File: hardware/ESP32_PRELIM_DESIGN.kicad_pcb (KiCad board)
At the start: 2 copper layers, 70 parts, among them J1 Conn_01x11_Socket, J4 Conn_01x02_Pin, J5 USB_C_Receptacle_USB2.0_16P, J6 Conn_01x05_Pin, J7 Conn_01x05_Pin, Q1 2N7002, SW1 SW_Push, SW2 SW_Push, SW3 SW_Push, U1 ESP32-S3-WROOM-1, U10 BQ24075RGT, U11 MAX98357A, U12 USBLC6-2SC6, U2 DRV2605LDGS, U3 TPS63020DSJR, U4 MAX17048G_T10

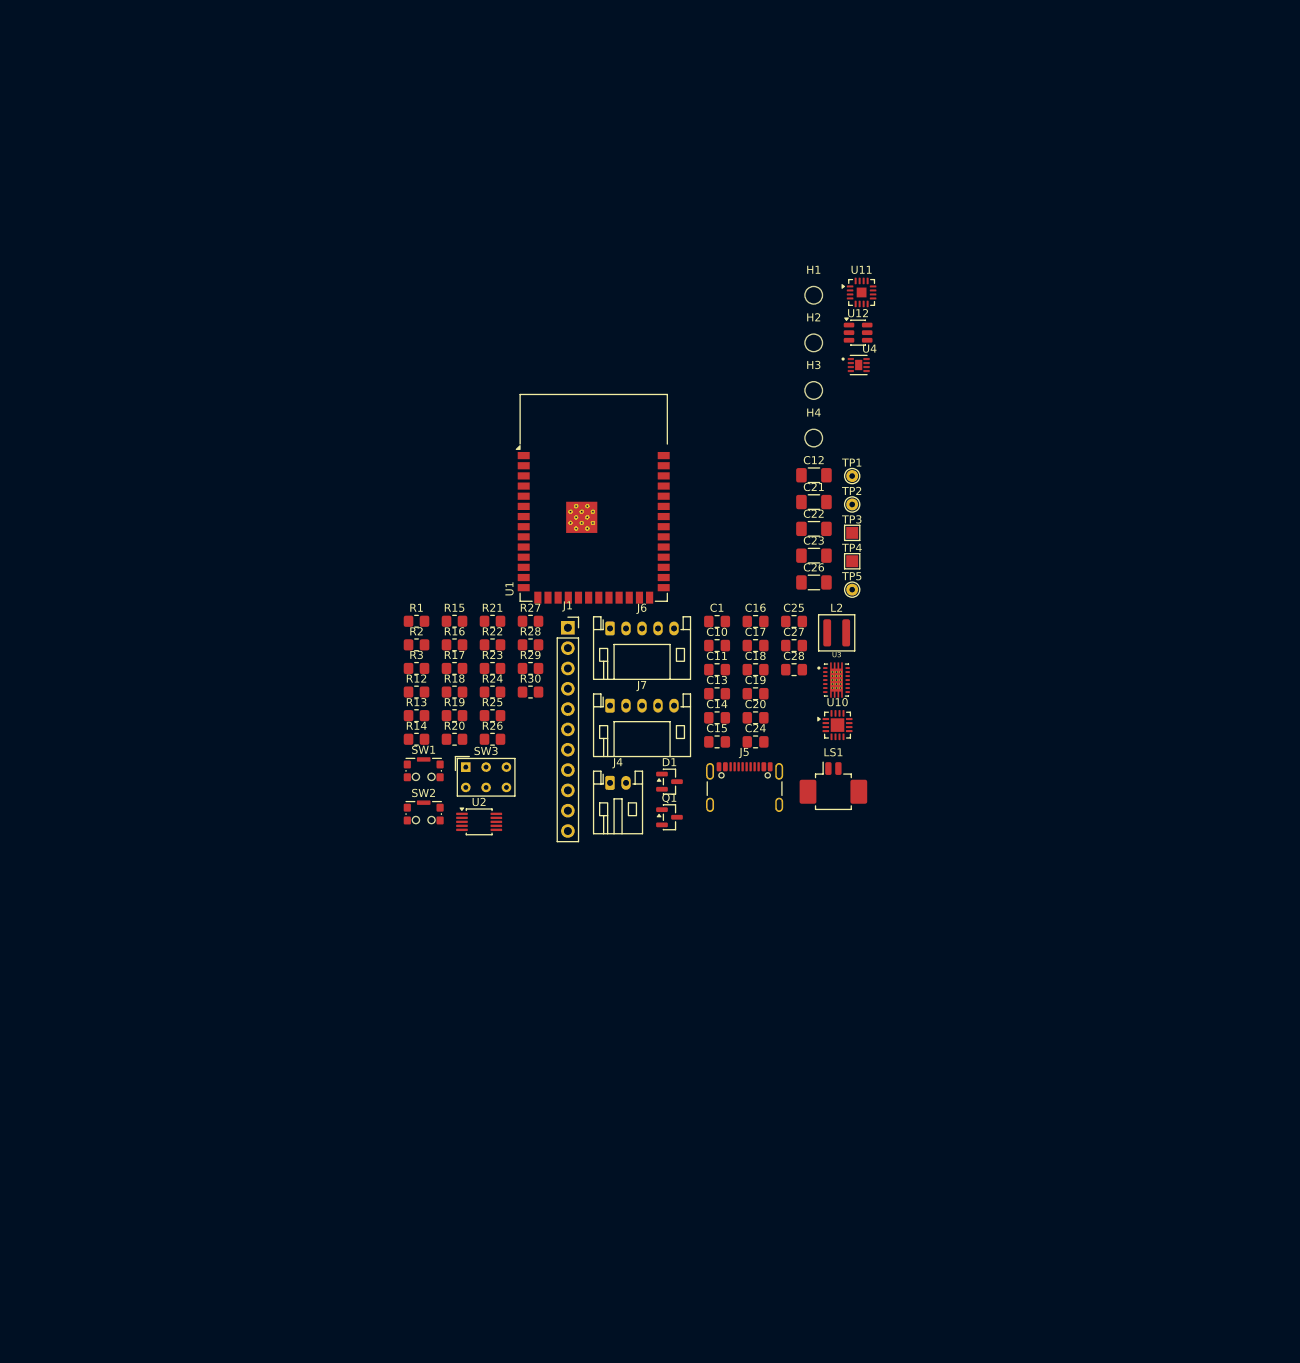
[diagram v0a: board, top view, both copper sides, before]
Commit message: pcb changes
isolated certain parts for better layout configuration
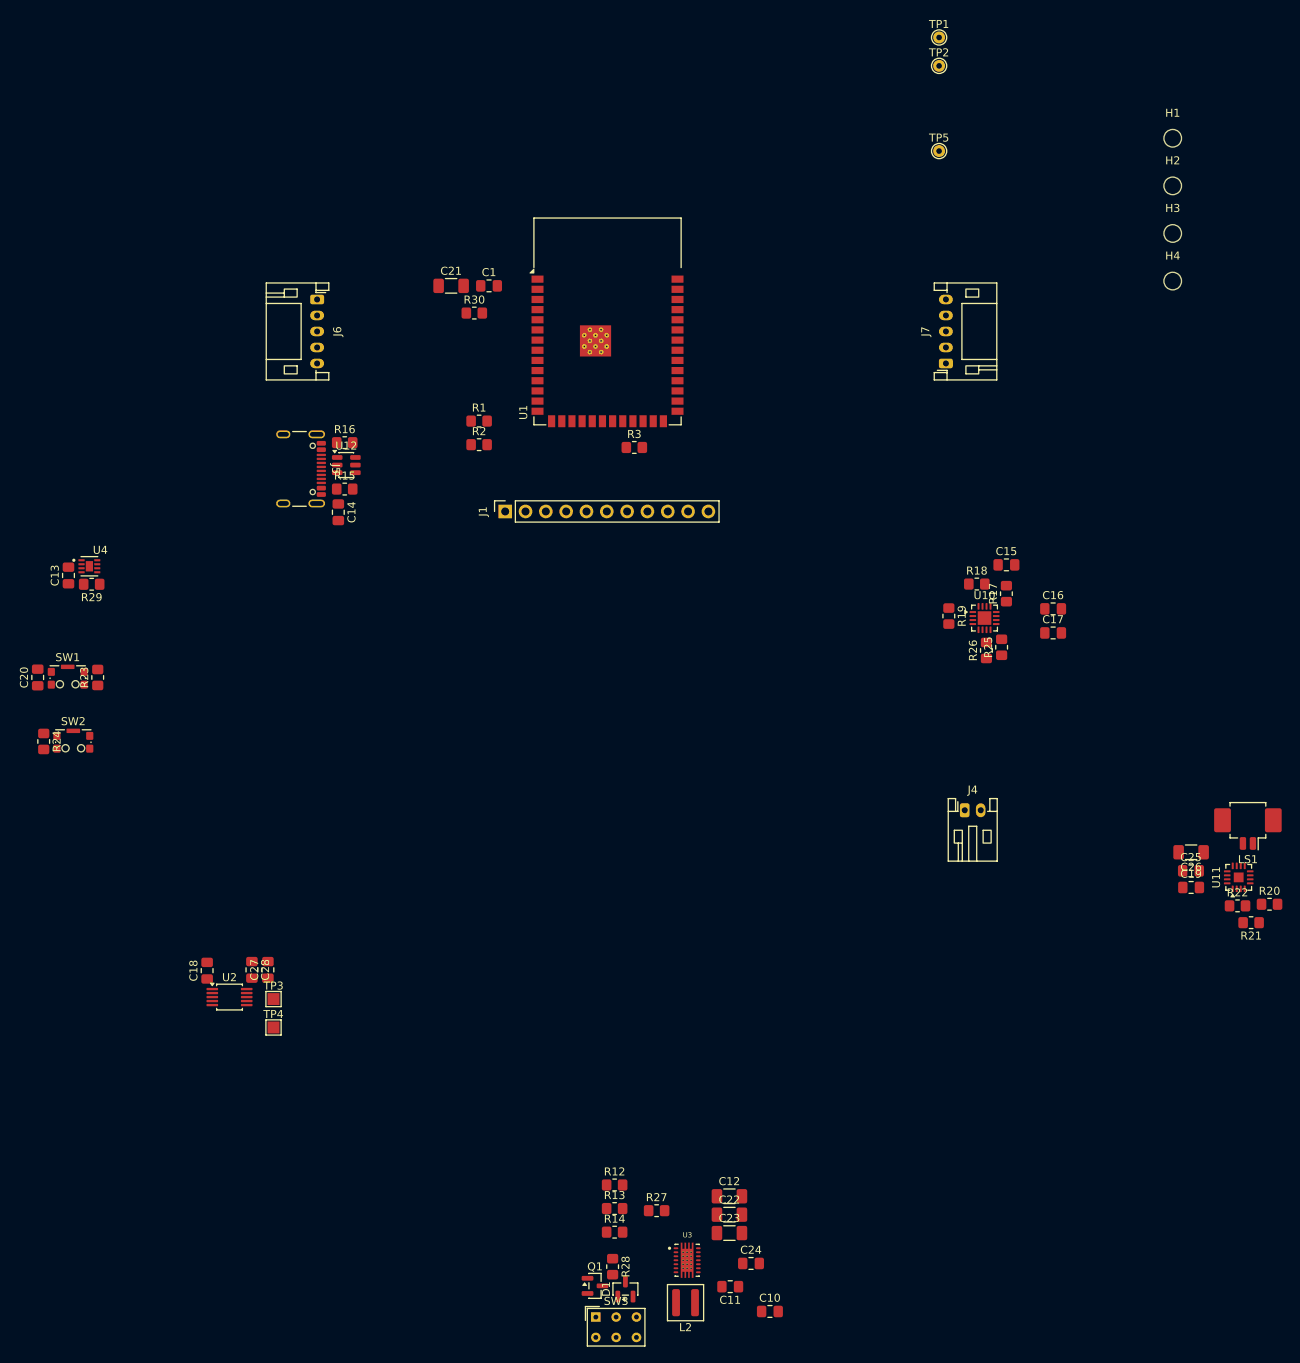
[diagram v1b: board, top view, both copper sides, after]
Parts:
- R18: value 1.13k -> 1.78k
- moved R20 103.9 mm to (188.5, 131.1)
- moved R21 102.0 mm to (186.2, 133.4), turned to 180 degrees
- moved U4 99.4 mm to (41.0, 88.8)
- moved R22 98.7 mm to (184.5, 131.3)
- moved TP4 92.9 mm to (64.0, 146.5)
- moved TP3 92.9 mm to (64.0, 142.9)
- moved C12 90.7 mm to (121.0, 167.6)
- moved C20 89.9 mm to (34.5, 102.8), turned to 90 degrees
- moved U11 87.0 mm to (184.7, 127.7), turned to 90 degrees
- moved C22 86.4 mm to (121.0, 169.9)
- moved L2 85.8 mm to (115.5, 180.9), turned to 180 degrees
- moved C23 85.3 mm to (121.0, 172.2)
- moved C10 83.5 mm to (126.0, 182.0)
- moved C13 82.4 mm to (38.4, 90.0), turned to 90 degrees
- moved R28 78.4 mm to (106.4, 176.4), turned to -90 degrees
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
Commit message: draft1pcb
draft 1 pcb schema
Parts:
- SW3: footprint Button_Switch_THT:SW_NKK_GW12LJP -> Button_Switch_SMD:SW_SPST_CK_KMS2xxGP
- TP1, TP2, TP5: moved to B.Cu
- moved J6 188.2 mm to (242.8, 128.9), turned to 90 degrees
- moved C20 172.1 mm to (205.5, 122.7), turned to 180 degrees
- moved SW1 168.2 mm to (205.7, 119.0), turned to -90 degrees
- moved R24 165.5 mm to (200.7, 115.2), turned to 180 degrees
- moved R23 163.9 mm to (205.5, 115.2), turned to 0 degrees
- moved SW2 162.1 mm to (200.8, 118.9), turned to 90 degrees
- moved C13 159.6 mm to (195.7, 117.3), turned to 180 degrees
- moved R29 157.2 mm to (196.8, 114.4), turned to -90 degrees
- moved U4 155.7 mm to (194.5, 114.7), turned to 90 degrees
- moved C18 146.0 mm to (198.2, 107.4), turned to -90 degrees
- moved U2 142.3 mm to (195.3, 103.5), turned to 180 degrees
- moved C28 137.9 mm to (195.2, 106.4), turned to 180 degrees
- moved C27 135.5 mm to (195.2, 108.4), turned to 0 degrees
- moved TP1 135.2 mm to (218.3, 137.8), turned to -90 degrees
- moved R1 134.4 mm to (214.2, 121.2), turned to 180 degrees
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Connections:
- J1 pad 10: /OLED_RST -> /SPI_CLK
- J1 pad 11: /SDCS -> /SPI_MOSI
- J1 pad 5: /SPI_CLK -> /MISO_SD
- J1 pad 6: /SPI_MOSI -> /SDCS
- J1 pad 7: /MISO_SD -> /OLED_CS
- J1 pad 8: /OLED_CS -> /OLED_RST
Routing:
- added copper zone on In2.Cu, net +3.3V
- added copper zone on B.Cu, net GND
- added copper zone on F.Cu, net GND
- added copper zone on In1.Cu, net GND
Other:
- board outline added: 70 x 40 mm
- copper layers 2 -> 4
- board text added: "Route VSYS and VBAT as wide traces (≥0.5 mm, 0.8 mm is better), mostly on F.Cu. This is the simplest option. Or add a VSYS region on In2, Signals on F.Cu return through the solid GND on In1. Keep these on top and over unbroken ground: USB D+/D− PDM_CLK and the I²S lines SPI_CLK Use B.Cu for slow lines: pull-ups, PWR_HOLD, CHG_STAT."

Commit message: pcb
pcb
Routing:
- net Net-(U1-EN): track 0.00 -> 15.1 mm, vias 0 -> 2
- net +3.3V: track 0.00 -> 7.32 mm
- net Net-(U1-IO4): track 0.00 -> 5.05 mm
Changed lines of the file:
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@@
 	)
 	(gr_text "Route VSYS and VBAT as wide traces (≥0.5 mm, 0.8 mm is better), mostly on F.Cu. This is the simplest option.\nOr add a VSYS region on In2,\n\nSignals on F.Cu return through the solid GND on In1. Keep these on top and over unbroken ground:\n\nUSB D+/D−\nPDM_CLK and the I²S lines\nSPI_CLK\n\nUse B.Cu for slow lines: pull-ups, PWR_HOLD, CHG_STAT."
-		(at 119.8 -8.3 0)
+		(at 113.3 63.25 0)
 		(layer "F.Cu")
 		(effects
@@
 		)
 	)
+	(segment
+		(start 207.0625 102.125)
+		(end 206.6375 101.7)
+		(width 0.2)
+		(layer "F.Cu")
+		(net "+3.3V")
+	)
+	(segment
+		(start 208.4025 102.76)
+		(end 207.0625 104.1)
+		(width 0.2)
+		(layer "F.Cu")
+		(net "+3.3V")
+	)
+	(segment
+		(start 207.0625 104.1)
+		(end 207.0625 102.125)
+		(width 0.2)
+		(layer "F.Cu")
+		(net "+3.3V")
+	)
+	(segment
+		(start 211.25 102.76)
+		(end 208.4025 102.76)
+		(width 0.2)
+		(layer "F.Cu")
+		(net "+3.3V")
+	)
+	(segment
+		(start 211.25 104.03)
+		(end 209.47 104.03)
+		(width 0.2)
+		(layer "F.Cu")
+		(net "Net-(U1-EN)")
+	)
+	(segment
+		(start 206.5 115.2)
+		(end 208.05 115.2)
+		(width 0.2)
+		(layer "F.Cu")
+		(net "Net-(U1-EN)")
+	)
+	(via
+		(at 208.05 115.2)
+		(size 0.6)
+		(drill 0.3)
+		(layers "F.Cu" "B.Cu")
+		(net "Net-(U1-EN)")
+	)
+	(via
+		(at 209.47 104.03)
+		(size 0.6)
+		(drill 0.3)
+		(layers "F.Cu" "B.Cu")
+		(net "Net-(U1-EN)")
+	)
+	(segment
+		(start 208.05 115.2)
+		(end 209.47 113.78)
+		(width 0.2)
+		(layer "B.Cu")
+		(net "Net-(U1-EN)")
+	)
+	(segment
+		(start 209.47 113.78)
+		(end 209.47 104.03)
+		(width 0.2)
+		(layer "B.Cu")
+		(net "Net-(U1-EN)")
+	)
+	(segment
+		(start 206.7 106.5)
+		(end 207.9 105.3)
+		(width 0.2)
+		(layer "F.Cu")
+		(net "Net-(U1-IO4)")
+	)
+	(segment
+		(start 207.9 105.3)
+		(end 211.25 105.3)
+		(width 0.2)
+		(layer "F.Cu")
+		(net "Net-(U1-IO4)")
+	)
 	(zone

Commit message: changes
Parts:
- moved R15 0.15 mm to (190.4, 113.5)
- moved TP1 0.10 mm to (218.3, 137.7)
- moved TP2 0.10 mm to (221.8, 137.7)
- moved TP5 0.10 mm to (225.5, 137.7)
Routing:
- net /TX: track 0.00 -> 50.7 mm, vias 0 -> 1
- net /SDCD: track 0.00 -> 46.2 mm, vias 0 -> 2
- net /RX: track 0.00 -> 45.0 mm, vias 0 -> 1
- net +3.3V: track 7.32 -> 29.1 mm
- net /SPI_MOSI: track 0.00 -> 19.8 mm, vias 0 -> 1
- net /SPI_CLK: track 0.00 -> 16.9 mm, vias 0 -> 1
- net /HAPTICS_EN: track 0.00 -> 16.5 mm
- net Net-(U11-OUTP): track 0.00 -> 15.2 mm, vias 0 -> 2
- net Net-(U3-VINA): track 0.00 -> 15.1 mm, vias 0 -> 2
- net GND: track 0.00 -> 14.1 mm, vias 0 -> 19
- net /PDM_CLK: track 0.00 -> 13.9 mm
- net /VBUS: track 0.00 -> 13.5 mm
- net /SDA: track 0.00 -> 13.2 mm
- net /SDCS: track 0.00 -> 13.1 mm, vias 0 -> 2
- net Net-(U11-OUTN): track 0.00 -> 12.0 mm
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
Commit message: changes
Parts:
- added D2: LED, LED_SMD:LED_0805_2012Metric_Pad1.15x1.40mm_HandSolder, F.Cu at (234.3, 102.0)
- added D3: LED, LED_SMD:LED_0805_2012Metric_Pad1.15x1.40mm_HandSolder, F.Cu at (234.3, 104.1)
- added D4: LED, LED_SMD:LED_0805_2012Metric_Pad1.15x1.40mm_HandSolder, F.Cu at (234.3, 106.2)
- added D5: LED, LED_SMD:LED_0805_2012Metric_Pad1.15x1.40mm_HandSolder, F.Cu at (234.3, 108.5)
- added H5: MountingHole, MountingHole:MountingHole_2.2mm_M2, F.Cu at (205.7, 147.2)
- added R4: 1.5k, Resistor_SMD:R_0805_2012Metric_Pad1.20x1.40mm_HandSolder, F.Cu at (238.2, 102.0)
- added R5: 1.5k, Resistor_SMD:R_0805_2012Metric_Pad1.20x1.40mm_HandSolder, F.Cu at (238.2, 104.1)
- added R6: 1.5k, Resistor_SMD:R_0805_2012Metric_Pad1.20x1.40mm_HandSolder, F.Cu at (238.2, 106.2)
- added R7: 1.5k, Resistor_SMD:R_0805_2012Metric_Pad1.20x1.40mm_HandSolder, F.Cu at (238.2, 108.5)
- added TP6: SDA, TestPoint:TestPoint_THTPad_D1.5mm_Drill0.7mm, B.Cu at (229.3, 155.4)
- added TP7: SCL, TestPoint:TestPoint_THTPad_D1.5mm_Drill0.7mm, B.Cu at (229.3, 158.9)
- added TP8: FG_ALRT, TestPoint:TestPoint_THTPad_D1.5mm_Drill0.7mm, B.Cu at (229.3, 162.5)
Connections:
- C27 pad 1: /VSYS -> +3.3V
- C28 pad 2: /VSYS -> +3.3V
- U1 pad 25: unconnected-(U1-IO48-Pad25) -> Net-(U1-IO48)
- U2 pad 10: /VSYS -> +3.3V

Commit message: pre DRC final layout
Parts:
- removed H3, H4, H5: MountingHole, MountingHole:MountingHole_2.2mm_M2
- TP1, TP2, TP5, TP6, TP7, TP8: footprint TestPoint:TestPoint_THTPad_D1.5mm_Drill0.7mm -> TestPoint:TestPoint_Pad_D2.0mm
- moved TP8 41.8 mm to (210.3, 125.2), turned to -90 degrees
- moved J1 36.8 mm to (243.0, 137.4), turned to 180 degrees
- moved TP7 36.0 mm to (216.8, 125.2), turned to -90 degrees
- moved R20 34.6 mm to (231.5, 102.4), turned to 90 degrees
- moved TP6 34.2 mm to (213.5, 125.1), turned to -90 degrees
- moved U11 32.6 mm to (236.6, 104.9), turned to 0 degrees
- moved LS1 31.4 mm to (242.5, 105.2), turned to 90 degrees
- moved R24 31.2 mm to (231.7, 118.7)
- moved SW2 31.2 mm to (231.8, 122.5)
- moved R21 30.7 mm to (233.5, 102.4)
- moved J6 30.1 mm to (212.9, 132.7), turned to 0 degrees
- moved C19 28.7 mm to (236.1, 108.0), turned to 0 degrees
- moved C25 28.3 mm to (236.1, 110.0), turned to 0 degrees
- moved R22 27.9 mm to (232.6, 105.3), turned to 0 degrees
- moved C26 27.9 mm to (239.2, 109.3)
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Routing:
- net +3.3V: track 29.1 -> 185.9 mm, vias 0 -> 7
- net /VSYS: track 2.05 -> 140.6 mm, vias 0 -> 7
- net /SCL: track 2.10 -> 61.8 mm, vias 0 -> 4
- net /CHG_STAT: track 4.49 -> 57.5 mm, vias 0 -> 2
- net /PGOOD: track 6.49 -> 57.3 mm, vias 0 -> 2
- net /PDM_DATA: track 0.00 -> 45.1 mm, vias 0 -> 2
- net /PWR_SENSE: track 0.00 -> 42.6 mm, vias 0 -> 3
- net /PWR_HOLD: track 0.00 -> 42.2 mm, vias 0 -> 3
- net /SDA: track 13.2 -> 49.5 mm, vias 0 -> 5
- net /I2S_LRCLK: track 0.00 -> 33.4 mm, vias 0 -> 2
- net /PDM_CLK: track 13.9 -> 46.3 mm, vias 0 -> 2
- net /FG_ALRT: track 0.00 -> 31.8 mm, vias 0 -> 5
- net /I2S_DOUT: track 0.00 -> 31.3 mm, vias 0 -> 2
- net /OLED_CS: track 10.3 -> 40.2 mm, vias 0 -> 1
- net /I2S_BCLK: track 0.00 -> 29.2 mm, vias 0 -> 2
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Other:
- board size 70 x 40 mm -> 66 x 40 mm
- board text removed: "Route VSYS and VBAT as wide traces (≥0.5 mm, 0.8 mm is better), mostly on F.Cu. This is the simplest option. Or add a VSYS region on In2, Signals on F.Cu return through the solid GND on In1. Keep these on top and over unbroken ground: USB D+/D− PDM_CLK and the I²S lines SPI_CLK Use B.Cu for slow lines: pull-ups, PWR_HOLD, CHG_STAT."

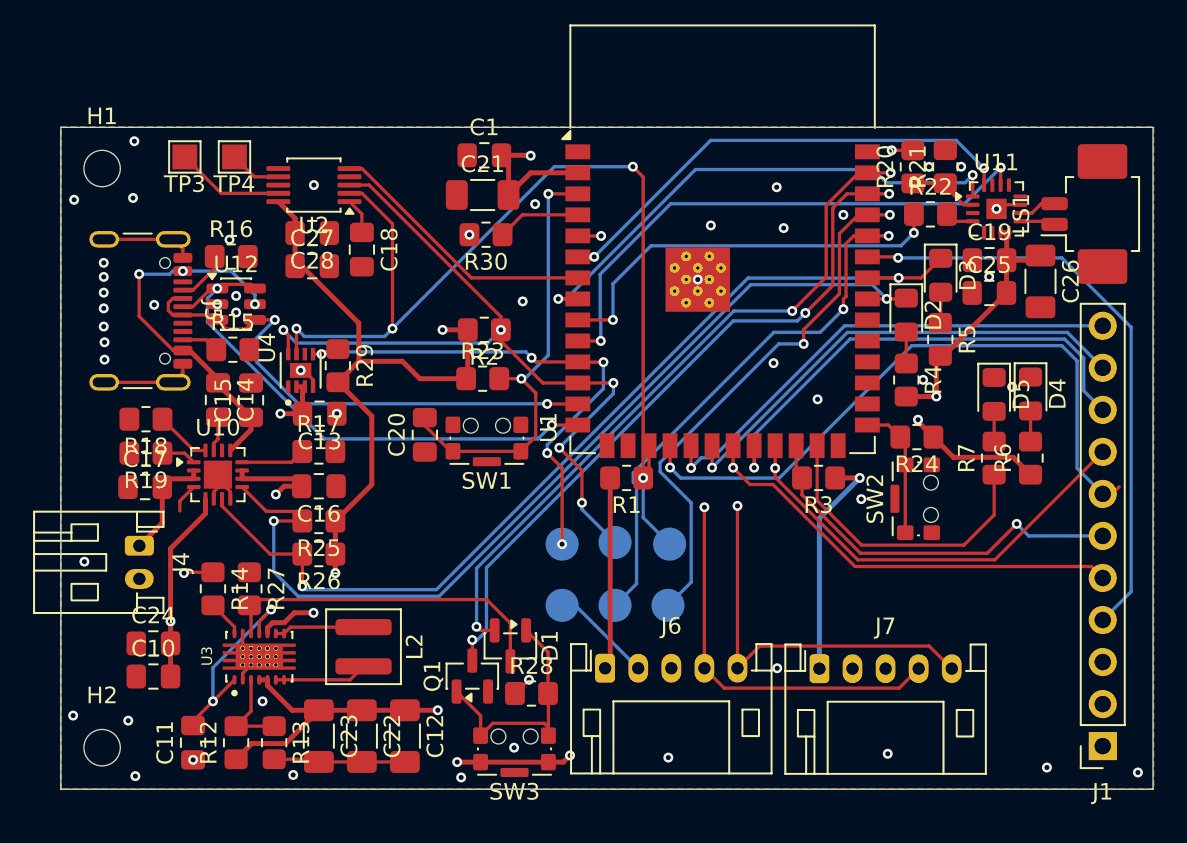
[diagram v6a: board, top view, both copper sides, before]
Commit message: pcb v1 post DRC (2 warnings)
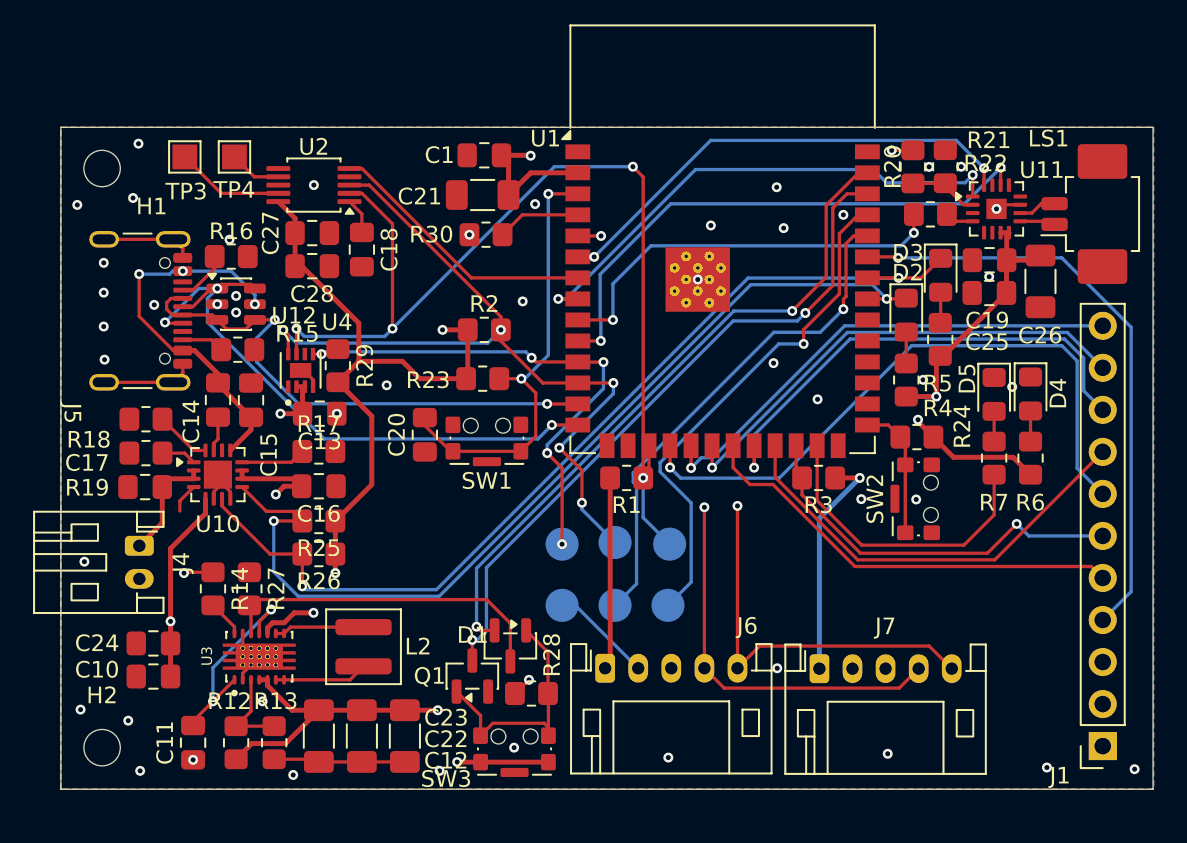
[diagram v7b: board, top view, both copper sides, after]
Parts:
- moved R15 0.30 mm to (190.7, 113.5)
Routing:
- net /USB_DP: track 33.0 -> 37.7 mm, vias 2 -> 3
- net /VSYS: track 140.6 -> 138.2 mm, vias 7 -> 6
- net GND: track 38.0 -> 35.9 mm, vias 55 -> 47
- net /PWR_HOLD: track 42.2 -> 40.2 mm, vias 3 -> 2
- net /TX: track 32.7 -> 30.8 mm, vias 2 -> 1
- net /OLED_CS: track 40.2 -> 38.6 mm
- net +3.3V: track 185.9 -> 184.3 mm
- net /PWR_SENSE: track 42.6 -> 41.3 mm, vias 3 -> 2
- net /RX: track 32.2 -> 30.9 mm, vias 2 -> 1
- net Net-(U3-EN): track 20.6 -> 19.9 mm
- net Net-(U1-EN): track 27.1 -> 26.5 mm
- net Net-(U11-~{SD_MODE}): track 1.73 -> 1.14 mm
- net /SDCS: track 23.8 -> 23.3 mm
- net /SCL: track 61.8 -> 61.3 mm
- net /OLED_RST: vias 1 -> 0
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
